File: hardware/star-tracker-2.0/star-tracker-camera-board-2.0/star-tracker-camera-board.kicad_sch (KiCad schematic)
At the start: 41 parts, among them J1 3-1734742-6, U1 AR0134CSSM00SPCA0, U2 TPS70618DRVR, U3 TPS71928-28DRVT, U4 TPS71928-28DRVT, X1 MC2520Z27.0000C19XSH

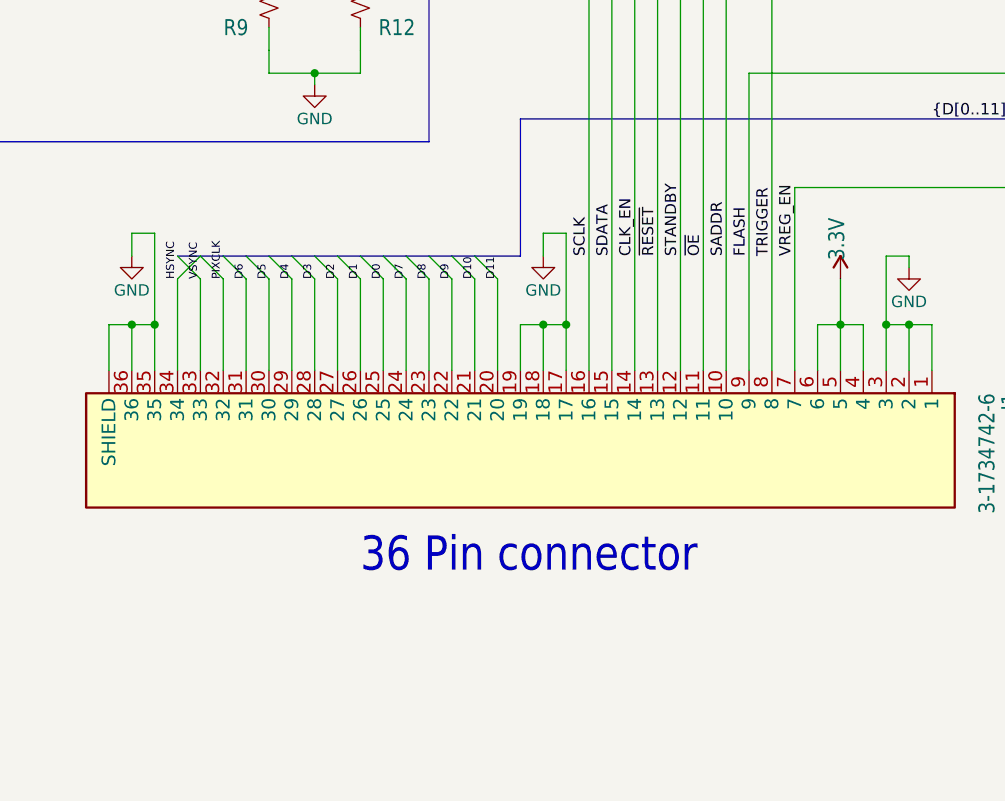
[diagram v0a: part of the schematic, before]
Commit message: Star tracker camera board
Fixing connector pin out so it fits on board well. Rotated sensor by 90 degrees. Started preliminary board layout
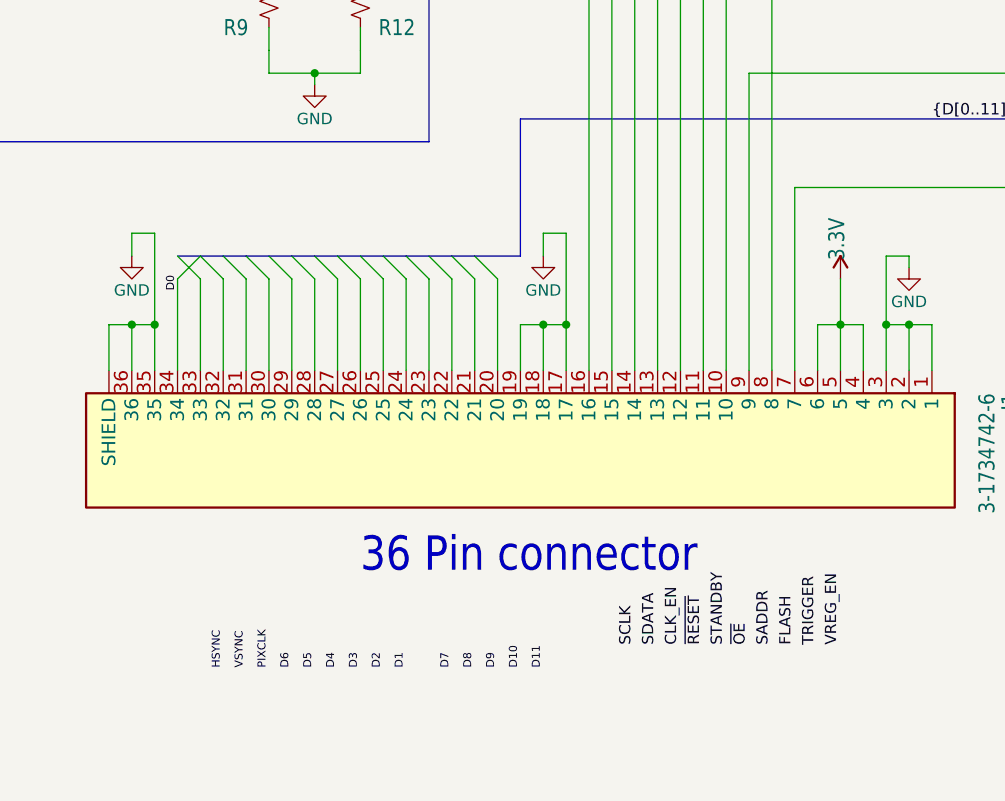
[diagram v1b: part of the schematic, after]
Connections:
- net D0: now also J1.34; no longer J1.25
- net D1: no longer J1.26
- net D10: no longer J1.21
- net D11: no longer J1.20
- net D2: no longer J1.27
- net D3: no longer J1.28
- net D4: no longer J1.29
- net D5: no longer J1.30
- net D6: no longer J1.31
- net D7: no longer J1.24
- net D8: no longer J1.23
- net D9: no longer J1.22
- net HSYNC: no longer J1.34
- net PIXCLK: no longer J1.32
- net VSYNC: no longer J1.33
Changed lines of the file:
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@@
+		)
+	)
+	(label "FLASH"
+		(at 137.16 226.06 90)
+		(effects
+			(font
+				(size 1.2446 1.2446)
+			)
+			(justify left bottom)
 		)
 	)
@@
 		)
 	)
-	(label "FLASH"
-		(at 132.08 182.88 90)
-		(effects
-			(font
-				(size 1.2446 1.2446)
-			)
-			(justify left bottom)
-		)
-	)
 	(label "D0"
 		(at 231.14 73.66 0)
@@
 		)
 	)
-	(label "D0"
-		(at 91.44 185.42 90)
-		(effects
-			(font
-				(size 0.889 0.889)
+	(label "TRIGGER"
+		(at 139.7 226.06 90)
+		(effects
+			(font
+				(size 1.2446 1.2446)
 			)
 			(justify left bottom)
@@
 		)
 	)
-	(label "D1"
-		(at 88.9 185.42 90)
-		(effects
-			(font
-				(size 0.889 0.889)
-			)
-			(justify left bottom)
-		)
-	)
-	(label "D7"
-		(at 93.98 185.42 90)
+	(label "D6"
+		(at 81.28 228.6 90)
 		(effects
 			(font
@@
 	)
 	(label "VREG_EN"
-		(at 137.16 182.88 90)
-		(effects
-			(font
-				(size 1.2446 1.2446)
+		(at 142.24 226.06 90)
+		(effects
+			(font
+				(size 1.2446 1.2446)
+			)
+			(justify left bottom)
+		)
+	)
+	(label "D4"
+		(at 86.36 228.6 90)
+		(effects
+			(font
+				(size 0.889 0.889)
 			)
 			(justify left bottom)
@@
 		)
 	)
-	(label "STANDBY"
-		(at 124.46 182.88 90)
-		(effects
-			(font
-				(size 1.2446 1.2446)
-			)
-			(justify left bottom)
-		)
-	)
-	(label "D4"
-		(at 81.28 185.42 90)
-		(effects
-			(font
-				(size 0.889 0.889)
-			)
-			(justify left bottom)
-		)
-	)
 	(label "SADDR"
 		(at 166.37 104.14 180)
@@
 		)
 	)
-	(label "SADDR"
-		(at 129.54 182.88 90)
-		(effects
-			(font
-				(size 1.2446 1.2446)
-			)
-			(justify left bottom)
-		)
-	)
-	(label "~{OE}"
-		(at 127 182.88 90)
-		(effects
-			(font
-				(size 1.2446 1.2446)
-			)
-			(justify left bottom)
-		)
-	)
-	(label "SDATA"
-		(at 116.84 182.88 90)
-		(effects
-			(font
-				(size 1.2446 1.2446)
+	(label "D9"
+		(at 104.14 228.6 90)
+		(effects
+			(font
+				(size 0.889 0.889)
+			)
+			(justify left bottom)
+		)
+	)
+	(label "SCLK"
+		(at 119.38 226.06 90)
+		(effects
+			(font
+				(size 1.2446 1.2446)
+			)
+			(justify left bottom)
+		)
+	)
+	(label "D10"
+		(at 106.68 228.6 90)
+		(effects
+			(font
+				(size 0.889 0.889)
 			)
 			(justify left bottom)
@@
 		)
 	)
-	(label "VSYNC"
-		(at 71.12 185.42 90)
-		(effects
-			(font
-				(size 0.889 0.889)
-			)
-			(justify left bottom)
-		)
-	)
-	(label "CLK_EN"
-		(at 119.38 182.88 90)
-		(effects
-			(font
-				(size 1.2446 1.2446)
-			)
-			(justify left bottom)
-		)
-	)
 	(label "D9"
 		(at 231.14 96.52 0)
@@
 		)
 	)
-	(label "D11"
-		(at 104.14 185.42 90)
+	(label "HSYNC"
+		(at 73.66 228.6 90)
 		(effects
 			(font
@@
 		)
 	)
-	(label "D6"
-		(at 76.2 185.42 90)
+	(label "D7"
+		(at 99.06 228.6 90)
+		(effects
+			(font
+				(size 0.889 0.889)
+			)
+			(justify left bottom)
+		)
+	)
+	(label "SADDR"
+		(at 134.62 226.06 90)
+		(effects
+			(font
+				(size 1.2446 1.2446)
+			)
+			(justify left bottom)
+		)
+	)
+	(label "D8"
+		(at 101.6 228.6 90)
 		(effects
 			(font
@@
 		)
 	)
+	(label "D2"
+		(at 91.44 228.6 90)
+		(effects
+			(font
+				(size 0.889 0.889)
+			)
+			(justify left bottom)
+		)
+	)
 	(label "D6"
 		(at 231.14 88.9 0)
@@
 		)
 	)
-	(label "PIXCLK"
-		(at 73.66 185.42 90)
+	(label "D5"
+		(at 83.82 228.6 90)
 		(effects
 			(font
@@
 		)
 	)
-	(label "D2"
-		(at 86.36 185.42 90)
-		(effects
-			(font
-				(size 0.889 0.889)
-			)
-			(justify left bottom)
-		)
-	)
 	(label "~{OE}"
 		(at 166.37 83.82 180)
@@
 		)
 	)
-	(label "D10"
-		(at 101.6 185.42 90)
+	(label "D3"
+		(at 88.9 228.6 90)
+		(effects
+			(font
+				(size 0.889 0.889)
+			)
+			(justify left bottom)
+		)
+	)
+	(label "CLK_EN"
+		(at 124.46 226.06 90)
+		(effects
+			(font
+				(size 1.2446 1.2446)
+			)
+			(justify left bottom)
+		)
+	)
+	(label "~{OE}"
+		(at 132.08 226.06 90)
+		(effects
+			(font
+				(size 1.2446 1.2446)
+			)
+			(justify left bottom)
+		)
+	)
+	(label "D1"
+		(at 93.98 228.6 90)
 		(effects
 			(font
@@
 		)
 	)
-	(label "TRIGGER"
-		(at 134.62 182.88 90)
+	(label "VSYNC"
+		(at 76.2 228.6 90)
+		(effects
+			(font
+				(size 0.889 0.889)
+			)
+			(justify left bottom)
+		)
+	)
+	(label "SDATA"
+		(at 121.92 226.06 90)
 		(effects
 			(font
@@
 		)
 	)
-	(label "D8"
-		(at 96.52 185.42 90)
-		(effects
-			(font
-				(size 0.889 0.889)
-			)
-			(justify left bottom)
-		)
-	)
 	(label "D11"
 		(at 231.14 101.6 0)
@@
 		)
 	)
-	(label "D5"
-		(at 78.74 185.42 90)
+	(label "D0"
+		(at 68.58 186.69 90)
 		(effects
 			(font
@@
 	)
 	(label "~{RESET}"
-		(at 121.92 182.88 90)
-		(effects
-			(font
-				(size 1.2446 1.2446)
-			)
-			(justify left bottom)
-		)
-	)
-	(label "SCLK"
-		(at 114.3 182.88 90)
-		(effects
-			(font
-				(size 1.2446 1.2446)
-			)
-			(justify left bottom)
-		)
-	)
-	(label "D9"
-		(at 99.06 185.42 90)
-		(effects
-			(font
-				(size 0.889 0.889)
-			)
-			(justify left bottom)
-		)
-	)
-	(label "HSYNC"
-		(at 68.58 185.42 90)
-		(effects
-			(font
-				(size 0.889 0.889)
+		(at 127 226.06 90)
+		(effects
+			(font
+				(size 1.2446 1.2446)
 			)
 			(justify left bottom)
@@
 		)
 	)
+	(label "STANDBY"
+		(at 129.54 226.06 90)
+		(effects
+			(font
+				(size 1.2446 1.2446)
+			)
+			(justify left bottom)
+		)
+	)
 	(label "PIXCLK"
 		(at 231.14 109.22 0)
@@
 		)
 	)
-	(label "D3"
-		(at 83.82 185.42 90)
-		(effects
-			(font
+	(label "PIXCLK"
+		(at 78.74 228.6 90)
+		(effects
+			(font
+				(size 0.889 0.889)
+			)
+			(justify left bottom)
+		)
+	)
+	(label "D11"
+		(at 109.22 228.6 90)
+		(effects
+			(font

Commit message: Cleaned up files
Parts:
- C10, C14, C6: DPN 490-GRT188R71E105KE13DCT-ND -> 490-18215-1-ND; MPN GRT188R71E105KE13D -> GRT155C81E105KE13D
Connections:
- net D0: now also J1.25; no longer J1.34
- net D1: now also J1.26
- net D10: now also J1.21
- net D11: now also J1.20
- net D2: now also J1.27
- net D3: now also J1.28
- net D4: now also J1.29
- net D5: now also J1.30
- net D6: now also J1.31
- net D7: now also J1.24
- net D8: now also J1.23
- net D9: now also J1.22
- net HSYNC: now also J1.34
- net PIXCLK: now also J1.32
- net VSYNC: now also J1.33

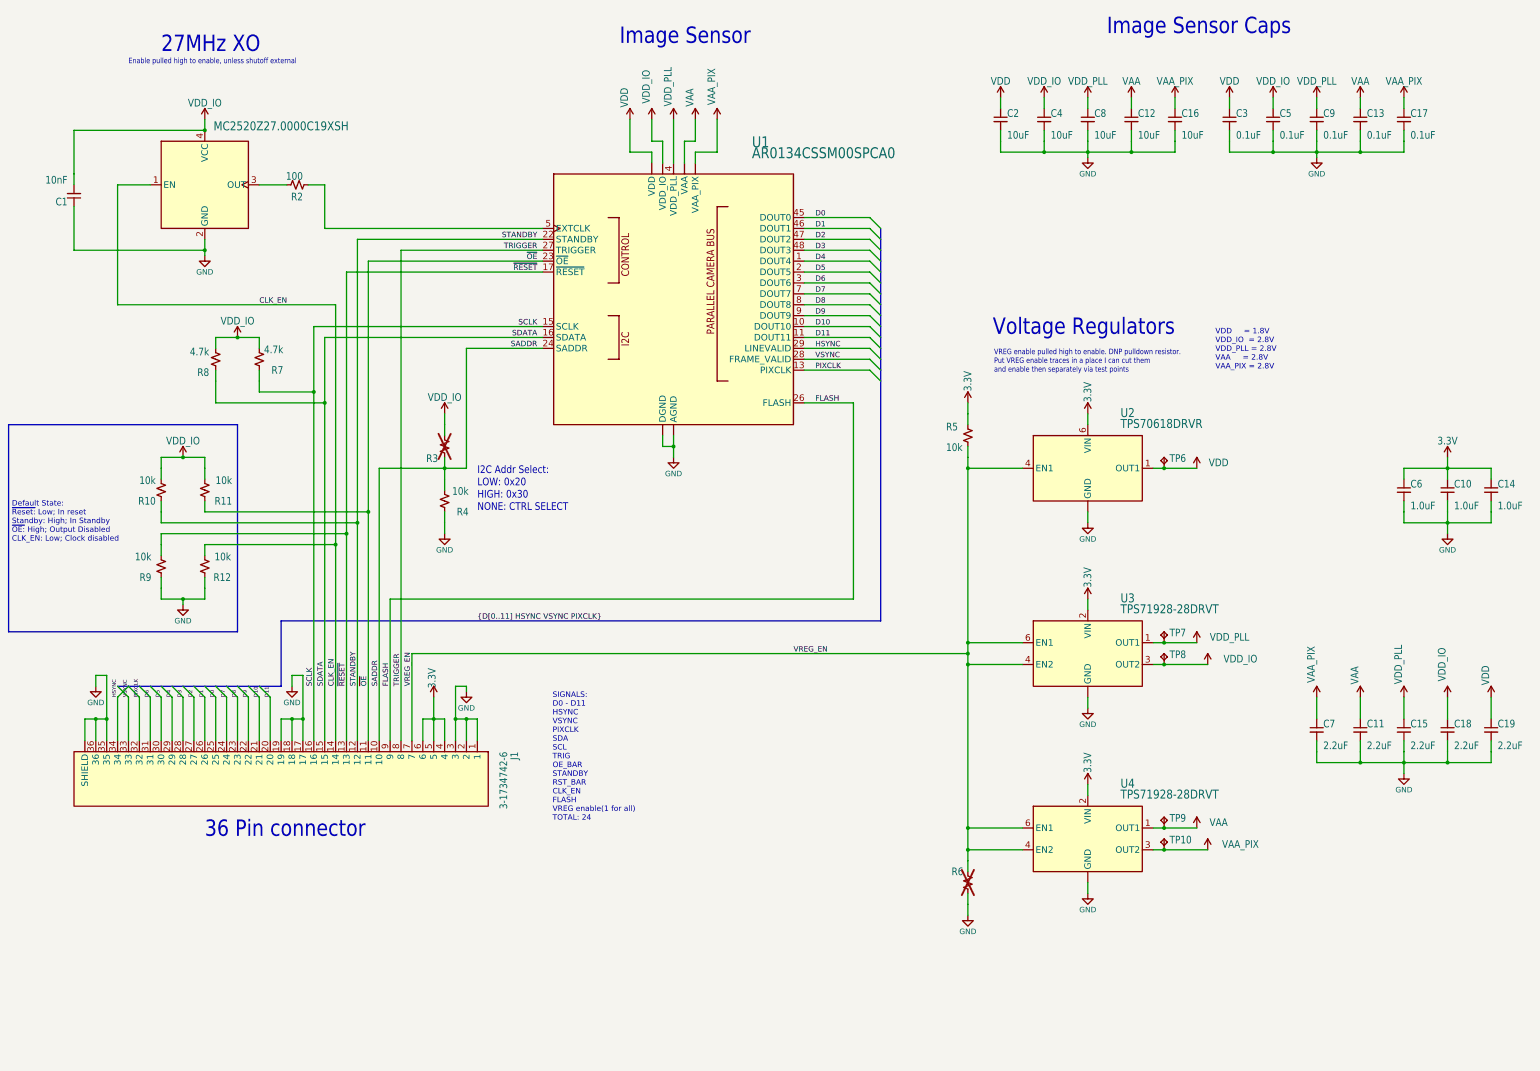
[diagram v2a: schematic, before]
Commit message: Update
Layout complete, 90% finished routing.
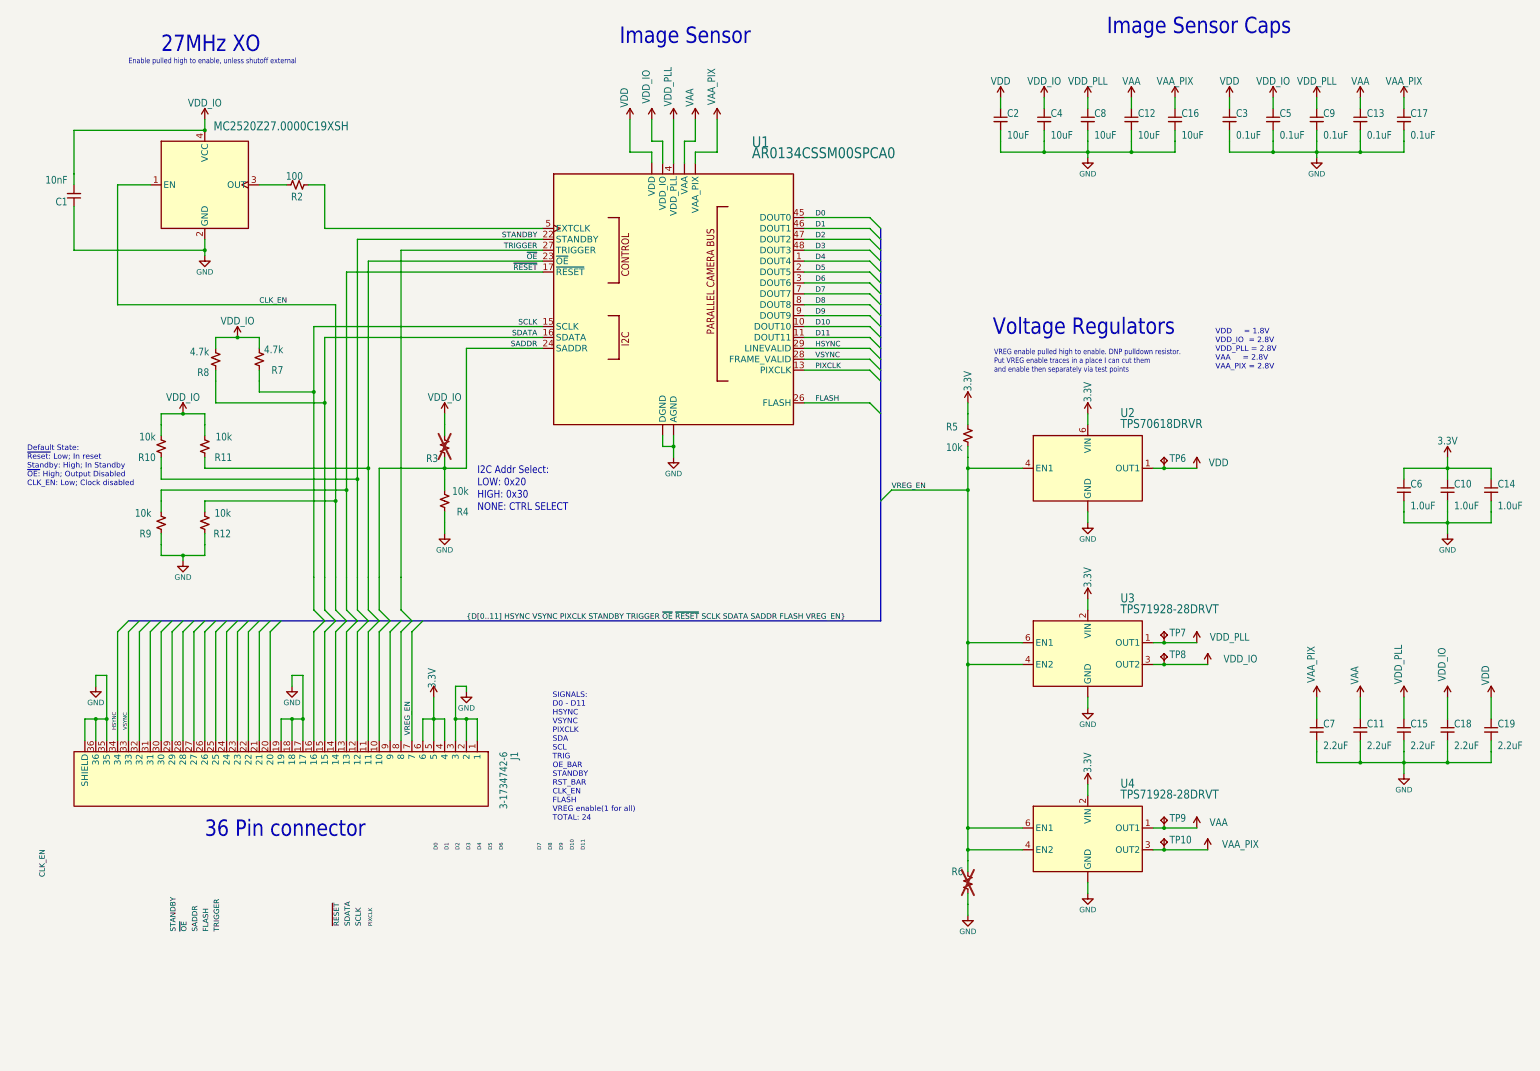
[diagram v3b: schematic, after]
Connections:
- net CLK_EN: no longer J1.14
- net D0: no longer J1.25
- net D1: no longer J1.26
- net D10: no longer J1.21
- net D11: no longer J1.20
- net D2: no longer J1.27
- net D3: no longer J1.28
- net D4: no longer J1.29
- net D5: no longer J1.30
- net D6: no longer J1.31
- net D7: no longer J1.24
- net D8: no longer J1.23
- net D9: no longer J1.22
- net FLASH: no longer J1.9
- net PIXCLK: no longer J1.32
- net SADDR: no longer J1.10
- net SCLK: no longer J1.16
- net SDATA: no longer J1.15
- net STANDBY: no longer J1.12
- net TRIGGER: no longer J1.8
- net ~{OE}: no longer J1.11
- net ~{RESET}: no longer J1.13
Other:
- moved on the sheet: R10, R11, R12, R9
